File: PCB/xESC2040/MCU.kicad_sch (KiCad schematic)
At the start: 20 parts, among them J6 Conn_01x02, U2 RP2040, U3 W25Q128JVS, Y1 Crystal

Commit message: WIP new power stage
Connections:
- net CUR_U is gone; now on net TEMP_MOTOR: U2.39 (GPIO27/ADC1)
- net CUR_V is gone; now on net AN_IN: U2.40 (GPIO28/ADC2)
- net AN_IN: no longer U2.38 (GPIO26/ADC0)
- net PCB_TEMP: now also U2.38 (GPIO26/ADC0); no longer U2.32 (GPIO21)
- net TEMP_MOTOR: no longer U2.37 (GPIO25)
- net CUR_W renamed CURRENT_SENSE
- net DRV_ENABLE: no longer names the net of U2.3 (GPIO1)
- net DRV_MISO: no longer names the net of U2.18 (GPIO15)
- net DRV_MOSI renamed SHUTDOWN
- net DRV_NCS renamed UART_TX
- net DRV_SCK renamed UART_RX
- net FAULT: no longer names the net of U2.4 (GPIO2)
- no-connect marks 6 -> 11
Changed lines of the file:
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@@
   (junction (at 177.8 39.37) (diameter 0) (color 0 0 0 0)
   )
+  (no_connect (at 110.49 110.49))
+  (no_connect (at 171.45 130.81))
+  (no_connect (at 171.45 118.11))
+  (no_connect (at 110.49 72.39))
+  (no_connect (at 110.49 74.93))
   (no_connect (at 110.49 69.85))
   (no_connect (at 110.49 82.55))
@@
     (effects (font (size 1.27 1.27)) (justify left))
   )
-  (hierarchical_label "DRV_MISO" (shape input) (at 110.49 110.49 180)
-    (effects (font (size 1.27 1.27)) (justify right))
-  )
-  (hierarchical_label "DRV_ENABLE" (shape output) (at 110.49 72.39 180)
+  (hierarchical_label "UART_RX" (shape input) (at 110.49 105.41 180)
     (effects (font (size 1.27 1.27)) (justify right))
   )
@@
     (effects (font (size 1.27 1.27)) (justify right))
   )
-  (hierarchical_label "TEMP_MOTOR" (shape input) (at 171.45 118.11 0)
+  (hierarchical_label "TEMP_MOTOR" (shape input) (at 171.45 113.03 0)
     (effects (font (size 1.27 1.27)) (justify left))
   )
@@
     (effects (font (size 1.27 1.27)) (justify right))
   )
-  (hierarchical_label "CUR_V" (shape input) (at 171.45 110.49 0)
-    (effects (font (size 1.27 1.27)) (justify left))
-  )
   (hierarchical_label "Reset" (shape input) (at 110.49 130.81 180)
     (effects (font (size 1.27 1.27)) (justify right))
@@
     (effects (font (size 1.27 1.27)) (justify right))
   )
-  (hierarchical_label "AN_IN" (shape input) (at 171.45 115.57 0)
-    (effects (font (size 1.27 1.27)) (justify left))
-  )
-  (hierarchical_label "CUR_U" (shape input) (at 171.45 113.03 0)
-    (effects (font (size 1.27 1.27)) (justify left))
-  )
-  (hierarchical_label "PCB_TEMP" (shape input) (at 171.45 130.81 0)
-    (effects (font (size 1.27 1.27)) (justify left))
-  )
-  (hierarchical_label "DRV_NCS" (shape output) (at 110.49 102.87 180)
-    (effects (font (size 1.27 1.27)) (justify right))
-  )
-  (hierarchical_label "FAULT" (shape input) (at 110.49 74.93 180)
-    (effects (font (size 1.27 1.27)) (justify right))
-  )
-  (hierarchical_label "DRV_SCK" (shape output) (at 110.49 105.41 180)
-    (effects (font (size 1.27 1.27)) (justify right))
+  (hierarchical_label "AN_IN" (shape input) (at 171.45 110.49 0)
+    (effects (font (size 1.27 1.27)) (justify left))
+  )
+  (hierarchical_label "PCB_TEMP" (shape input) (at 171.45 115.57 0)
+    (effects (font (size 1.27 1.27)) (justify left))
   )
   (hierarchical_label "HALL_1" (shape input) (at 171.45 120.65 0)
@@
     (effects (font (size 1.27 1.27)) (justify left))
   )
-  (hierarchical_label "DRV_MOSI" (shape output) (at 110.49 107.95 180)
+  (hierarchical_label "UART_TX" (shape output) (at 110.49 102.87 180)
     (effects (font (size 1.27 1.27)) (justify right))
   )
@@
     (effects (font (size 1.27 1.27)) (justify right))
   )
-  (hierarchical_label "CUR_W" (shape input) (at 171.45 107.95 0)
-    (effects (font (size 1.27 1.27)) (justify left))
+  (hierarchical_label "CURRENT_SENSE" (shape input) (at 171.45 107.95 0)
+    (effects (font (size 1.27 1.27)) (justify left))
+  )
+  (hierarchical_label "SHUTDOWN" (shape input) (at 110.49 107.95 180)
+    (effects (font (size 1.27 1.27)) (justify right))
   )
   (hierarchical_label "UH" (shape output) (at 110.49 100.33 180)

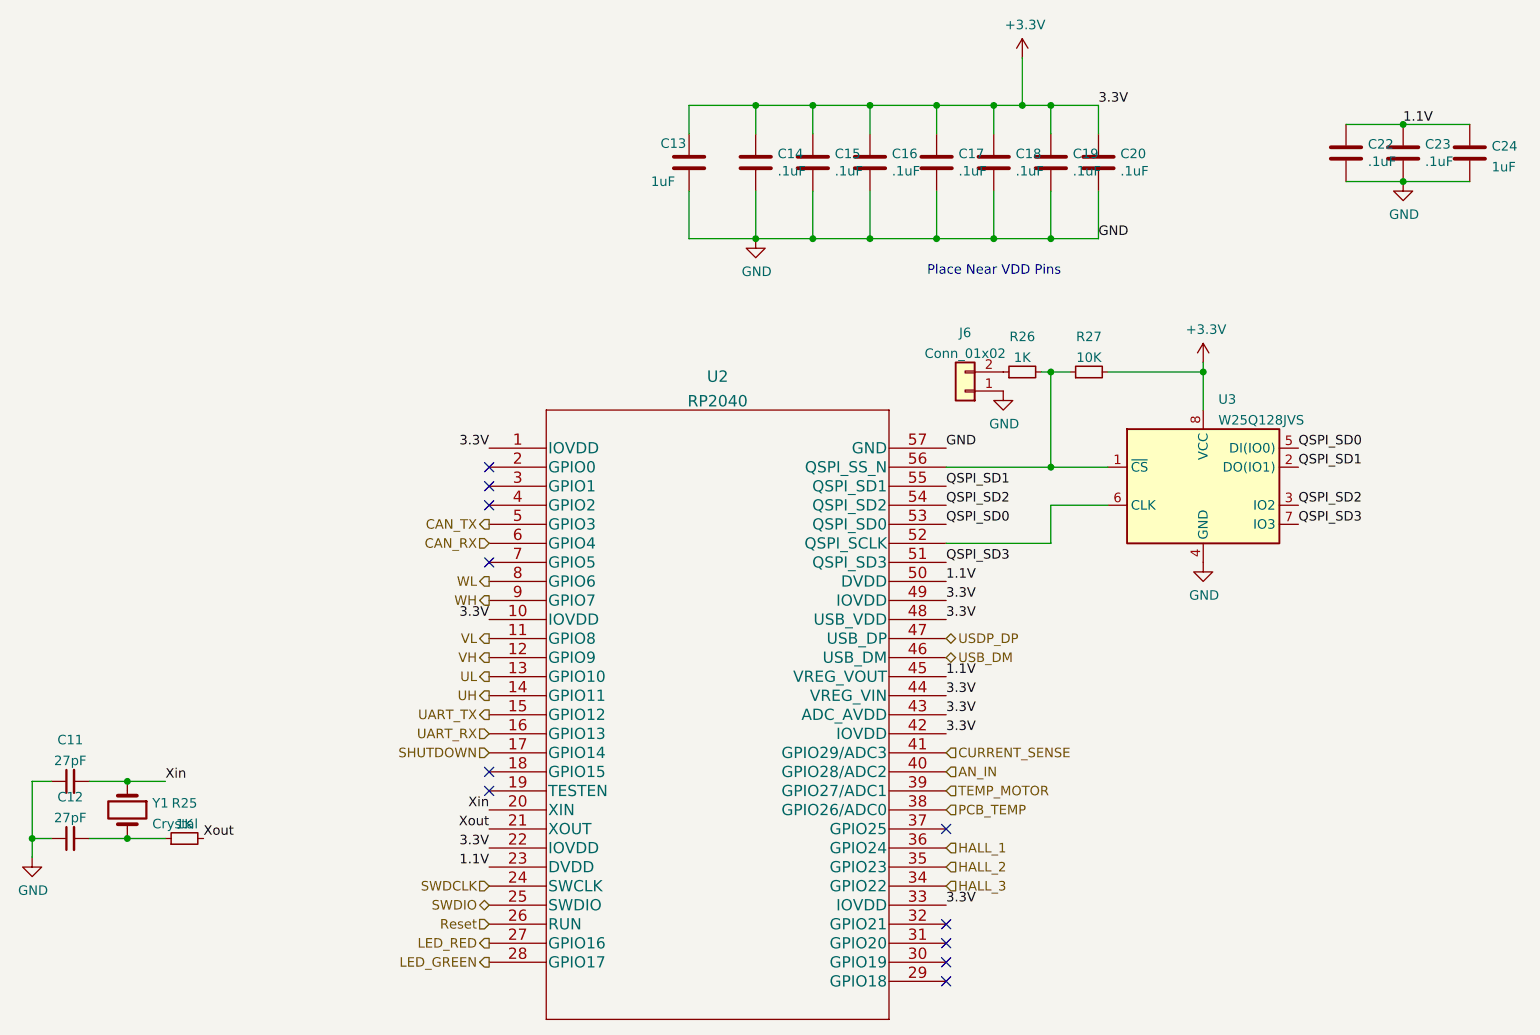
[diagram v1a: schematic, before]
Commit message: wip - all parts placed some routing left
Only schematic change was the spi flash change to a  smaller footprint version of the same part W25Q128JVS->W25Q128JVP and GPIO remapping to simplify routing.  Layout has optional CAN parts on bottom but rest fits on top.
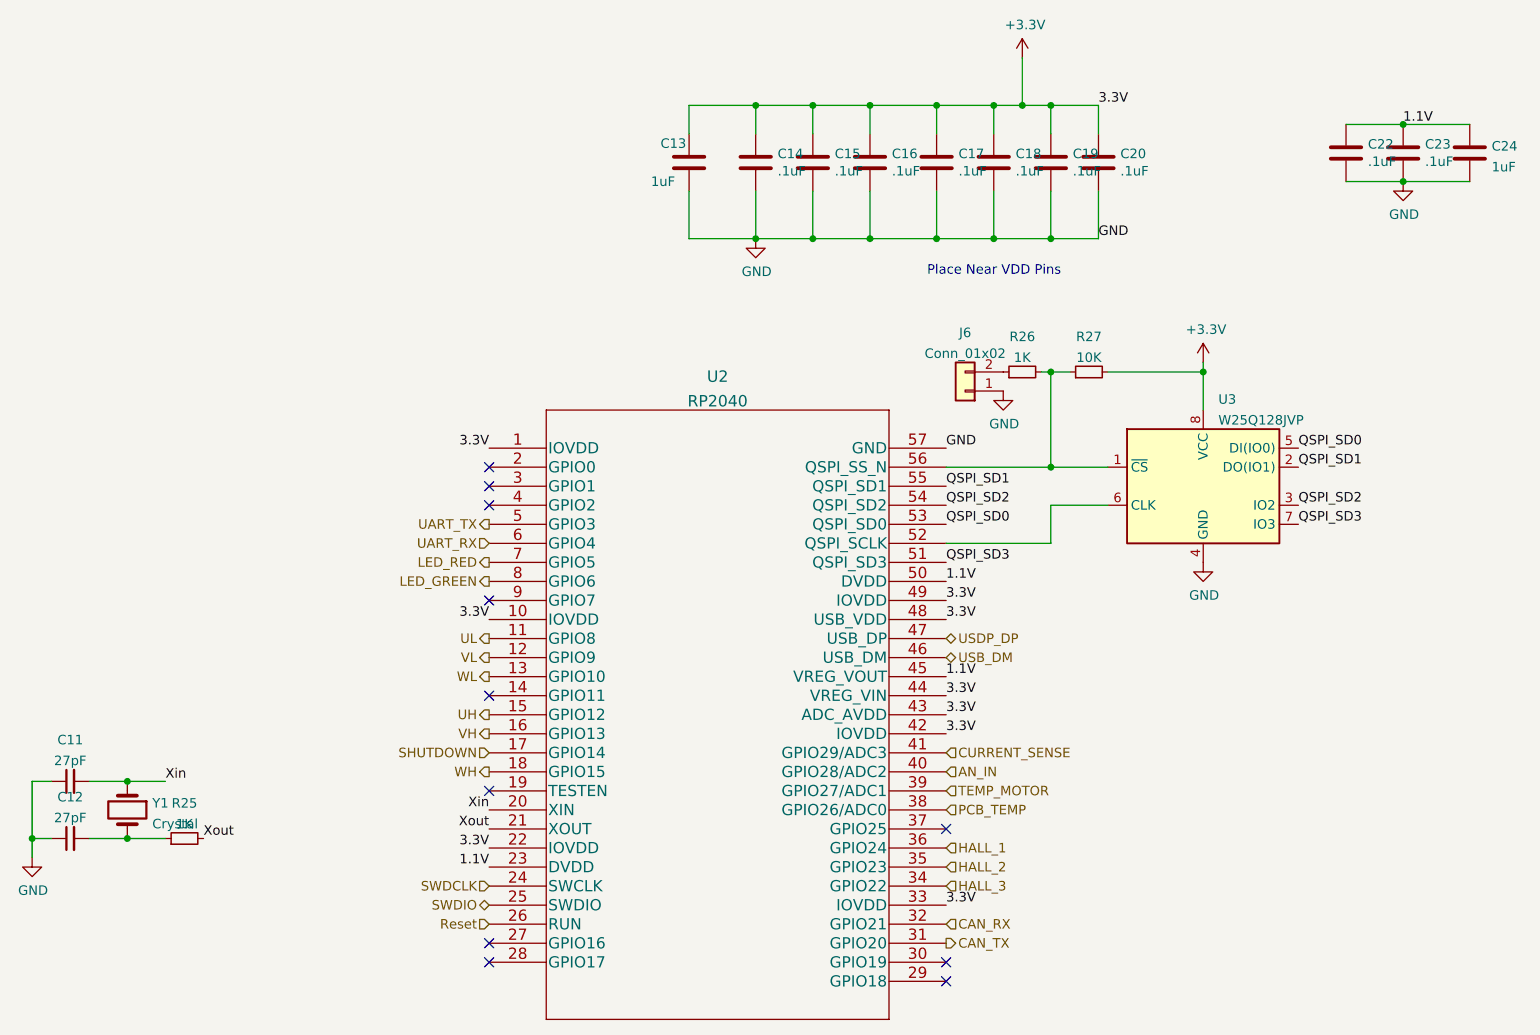
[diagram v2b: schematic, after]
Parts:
- U3: value W25Q128JVS -> W25Q128JVP; footprint Package_SO:SOIC-8_5.23x5.23mm_P1.27mm -> Package_SON:WSON-8-1EP_6x5mm_P1.27mm_EP3.4x4.3mm
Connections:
- net CAN_RX: now also U2.32 (GPIO21); no longer U2.6 (GPIO4)
- net CAN_TX: now also U2.31 (GPIO20); no longer U2.5 (GPIO3)
- net LED_GREEN: now also U2.8 (GPIO6); no longer U2.28 (GPIO17)
- net LED_RED: now also U2.7 (GPIO5); no longer U2.27 (GPIO16)
- net UART_RX: now also U2.6 (GPIO4); no longer U2.16 (GPIO13)
- net UART_TX: now also U2.5 (GPIO3); no longer U2.15 (GPIO12)
- net UH: now also U2.15 (GPIO12); no longer U2.14 (GPIO11)
- net UL: now also U2.11 (GPIO8); no longer U2.13 (GPIO10)
- net VH: now also U2.16 (GPIO13); no longer U2.12 (GPIO9)
- net VL: now also U2.12 (GPIO9); no longer U2.11 (GPIO8)
- net WH: now also U2.18 (GPIO15); no longer U2.9 (GPIO7)
- net WL: now also U2.13 (GPIO10); no longer U2.8 (GPIO6)
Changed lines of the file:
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@@
   (junction (at 177.8 39.37) (diameter 0) (color 0 0 0 0)
   )
-  (no_connect (at 110.49 110.49))
-  (no_connect (at 171.45 130.81))
+  (no_connect (at 110.49 100.33))
+  (no_connect (at 110.49 133.35))
   (no_connect (at 171.45 118.11))
   (no_connect (at 110.49 72.39))
   (no_connect (at 110.49 74.93))
   (no_connect (at 110.49 69.85))
-  (no_connect (at 110.49 82.55))
+  (no_connect (at 110.49 87.63))
   (no_connect (at 110.49 113.03))
   (no_connect (at 171.45 138.43))
   (no_connect (at 171.45 135.89))
-  (no_connect (at 171.45 133.35))
+  (no_connect (at 110.49 135.89))
   (wire (pts (xy 185.42 74.93) (xy 185.42 80.01))
     (stroke (width 0) (type default) (color 0 0 0 0))
@@
     (effects (font (size 1.27 1.27)) (justify left bottom))
   )
-  (hierarchical_label "CAN_TX" (shape output) (at 110.49 77.47 180)
-    (effects (font (size 1.27 1.27)) (justify right))
+  (hierarchical_label "CAN_TX" (shape output) (at 171.45 133.35 0)
+    (effects (font (size 1.27 1.27)) (justify left))
   )
   (hierarchical_label "USDP_DP" (shape bidirectional) (at 171.45 92.71 0)
     (effects (font (size 1.27 1.27)) (justify left))
   )
-  (hierarchical_label "UART_RX" (shape input) (at 110.49 105.41 180)
-    (effects (font (size 1.27 1.27)) (justify right))
-  )
-  (hierarchical_label "CAN_RX" (shape input) (at 110.49 80.01 180)
-    (effects (font (size 1.27 1.27)) (justify right))
+  (hierarchical_label "UART_RX" (shape input) (at 110.49 80.01 180)
+    (effects (font (size 1.27 1.27)) (justify right))
+  )
+  (hierarchical_label "CAN_RX" (shape input) (at 171.45 130.81 0)
+    (effects (font (size 1.27 1.27)) (justify left))
   )
   (hierarchical_label "TEMP_MOTOR" (shape input) (at 171.45 113.03 0)
     (effects (font (size 1.27 1.27)) (justify left))
   )
-  (hierarchical_label "UL" (shape output) (at 110.49 97.79 180)
+  (hierarchical_label "UL" (shape output) (at 110.49 92.71 180)
     (effects (font (size 1.27 1.27)) (justify right))
   )
@@
     (effects (font (size 1.27 1.27)) (justify right))
   )
-  (hierarchical_label "VH" (shape output) (at 110.49 95.25 180)
+  (hierarchical_label "VH" (shape output) (at 110.49 105.41 180)
     (effects (font (size 1.27 1.27)) (justify right))
   )
@@
     (effects (font (size 1.27 1.27)) (justify right))
   )
-  (hierarchical_label "WH" (shape output) (at 110.49 87.63 180)
+  (hierarchical_label "WH" (shape output) (at 110.49 110.49 180)
     (effects (font (size 1.27 1.27)) (justify right))
   )
@@
     (effects (font (size 1.27 1.27)) (justify left))
   )
-  (hierarchical_label "UART_TX" (shape output) (at 110.49 102.87 180)
+  (hierarchical_label "UART_TX" (shape output) (at 110.49 77.47 180)
     (effects (font (size 1.27 1.27)) (justify right))
   )
@@
     (effects (font (size 1.27 1.27)) (justify right))
   )
-  (hierarchical_label "UH" (shape output) (at 110.49 100.33 180)
-    (effects (font (size 1.27 1.27)) (justify right))
-  )
-  (hierarchical_label "WL" (shape output) (at 110.49 85.09 180)
-    (effects (font (size 1.27 1.27)) (justify right))
-  )
-  (hierarchical_label "LED_RED" (shape output) (at 110.49 133.35 180)
+  (hierarchical_label "UH" (shape output) (at 110.49 102.87 180)
+    (effects (font (size 1.27 1.27)) (justify right))
+  )
+  (hierarchical_label "WL" (shape output) (at 110.49 97.79 180)
+    (effects (font (size 1.27 1.27)) (justify right))
+  )
+  (hierarchical_label "LED_RED" (shape output) (at 110.49 82.55 180)
     (effects (font (size 1.27 1.27)) (justify right))
   )
@@
     (effects (font (size 1.27 1.27)) (justify left))
   )
-  (hierarchical_label "VL" (shape output) (at 110.49 92.71 180)
-    (effects (font (size 1.27 1.27)) (justify right))
-  )
-  (hierarchical_label "LED_GREEN" (shape output) (at 110.49 135.89 180)
+  (hierarchical_label "VL" (shape output) (at 110.49 95.25 180)
+    (effects (font (size 1.27 1.27)) (justify right))
+  )
+  (hierarchical_label "LED_GREEN" (shape output) (at 110.49 85.09 180)
     (effects (font (size 1.27 1.27)) (justify right))
   )
@@
       (effects (font (size 1.27 1.27)) (justify left))
     )
-    (property "Value" "W25Q128JVS" (id 1) (at 207.7594 63.5786 0)
-      (effects (font (size 1.27 1.27)) (justify left))
-    )
-    (property "Footprint" "Package_SO:SOIC-8_5.23x5.23mm_P1.27mm" (id 2) (at 205.74 72.39 0)
-      (effects (font (size 1.27 1.27)) hide)
-    )
+    (property "Value" "W25Q128JVP" (id 1) (at 207.7594 63.5786 0)
+      (effects (font (size 1.27 1.27)) (justify left))
+    )
+    (property "Footprint" "Package_SON:WSON-8-1EP_6x5mm_P1.27mm_EP3.4x4.3mm" (id 2) (at 205.74 72.39 0)
+      (effects (font (size 1.27 1.27)) hide)
+    )
